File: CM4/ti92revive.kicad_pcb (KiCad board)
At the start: 2 copper layers, 205 x 116.7 mm, 200 parts, among them J1 USB_B, J2 Conn_01x02, J3 Conn_01x02, U1 Compute_Module_4_Connectors, U2 Compute_Module_4_Connectors, U3 BQ25887RGET

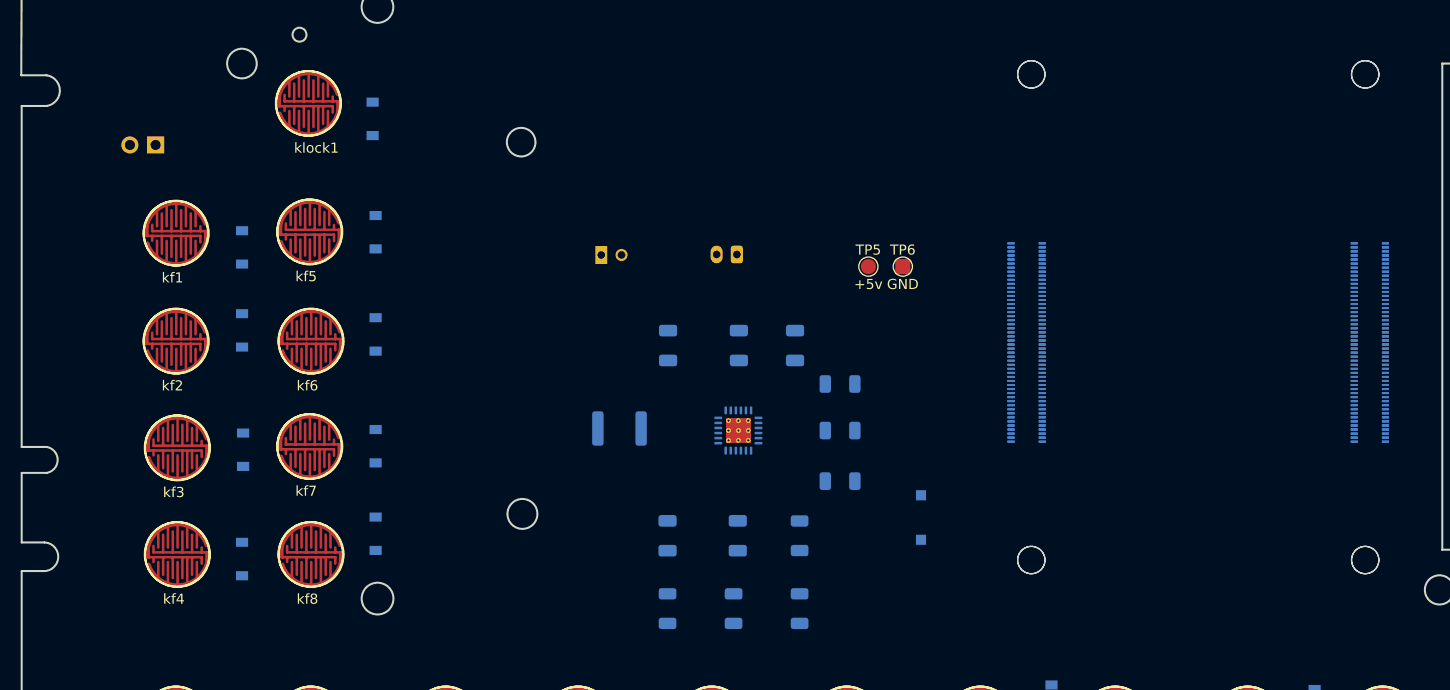
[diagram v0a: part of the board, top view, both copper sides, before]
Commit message: Laid out 5v ic and battery charger
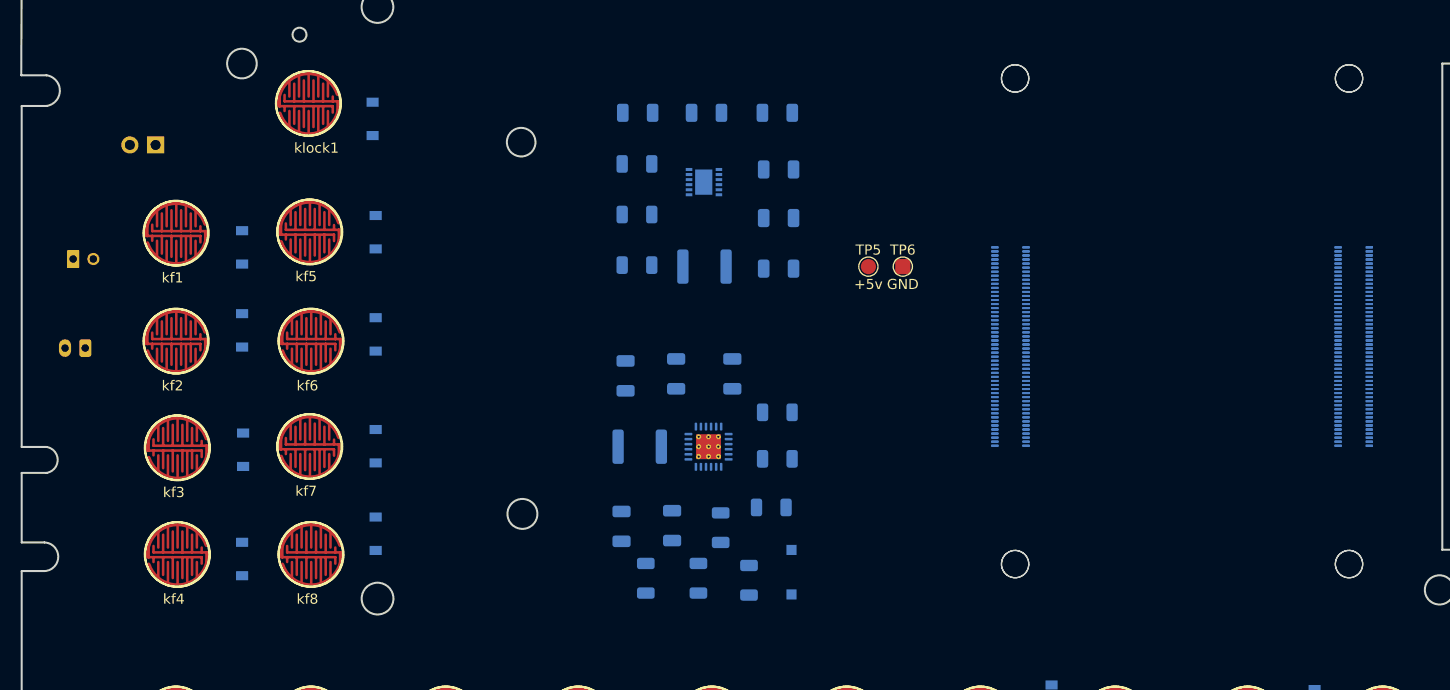
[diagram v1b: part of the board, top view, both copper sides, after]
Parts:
- added C10: .1uF, Capacitor_SMD:C_1206_3216Metric, B.Cu at (120.4, 50.8)
- added C11: 22uF, Capacitor_SMD:C_1206_3216Metric, B.Cu at (113.6, 50.8)
- added C6: 5.6nF, Capacitor_SMD:C_1206_3216Metric, B.Cu at (127.5, 61.2)
- added C7: 2.2uF, Capacitor_SMD:C_1206_3216Metric, B.Cu at (127.5, 56.4)
- added C8: 2.2uF, Capacitor_SMD:C_1206_3216Metric, B.Cu at (127.5, 66.2)
- added C9: .1uF, Capacitor_SMD:C_1206_3216Metric, B.Cu at (127.4, 50.8)
- added L2: 10uH, Inductor_SMD:L_1812_4532Metric, B.Cu at (120.2, 66.0)
- added R10: 105K, Resistor_SMD:R_1206_3216Metric, B.Cu at (113.5, 65.8)
- added R11: 23.2K, Resistor_SMD:R_1206_3216Metric, B.Cu at (113.5, 60.9)
- added R9: 4.7, Resistor_SMD:R_1206_3216Metric, B.Cu at (113.5, 55.9)
- added U4: MAX17643, trinamic-footprints:TDFN-12_3x3mm_P0.5mm, B.Cu at (120.1, 57.6)
- moved J3 65.1 mm to (59.0, 74.0)
- moved J2 52.2 mm to (59.8, 65.2)
- moved TP11 16.1 mm to (128.8, 98.4)
- moved TP10 12.8 mm to (128.8, 94.0)
- moved R8 10.4 mm to (119.6, 96.8)
- moved R4 9.18 mm to (114.4, 96.8)
- moved R1 8.52 mm to (124.6, 97.0)
- moved R2 7.84 mm to (121.8, 91.8)
- moved R3 7.28 mm to (126.8, 89.8)
- moved C4 6.80 mm to (123.0, 76.6)
- moved R6 6.80 mm to (127.4, 80.4)
- moved C2 6.80 mm to (117.4, 76.6)
- moved R5 6.80 mm to (127.4, 85.0)
- moved C1 6.57 mm to (117.0, 91.6)
- moved C5 5.16 mm to (112.4, 76.8)
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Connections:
- J1 pad 5: unconnected-(J1-Pad5) -> GND

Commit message: Added Power Button Control Circuit
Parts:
- added D82: PWR IND, LED_SMD:LED_2010_5025Metric, F.Cu at (243.0, 38.8)
- added JP1: Oopes just use a switch, Jumper:SolderJumper-2_P1.3mm_Open_RoundedPad1.0x1.5mm, B.Cu at (105.8, 67.0)
- added Q1: Q_NPN_BCE, Package_TO_SOT_SMD:SOT-23, B.Cu at (100.2, 66.8)
- added R12: 330, Resistor_SMD:R_1206_3216Metric, B.Cu at (99.2, 72.4)
- added R13: 330, Resistor_SMD:R_1206_3216Metric, B.Cu at (99.2, 77.6)
- added U5: ATTINY85-20PU, digikey-footprints:DIP-8_W7.62mm, B.Cu at (111.6, 71.2)
- D81: footprint LED_SMD:LED_1206_3216Metric -> LED_SMD:LED_2010_5025Metric
- moved C11 14.3 mm to (125.8, 43.4)
- moved L2 14.3 mm to (132.4, 58.6)
- moved C6 14.3 mm to (139.7, 53.8)
- moved C8 14.3 mm to (139.7, 58.8)
- moved C10 14.3 mm to (132.6, 43.4)
- moved C7 14.3 mm to (139.7, 49.0)
- moved C9 14.3 mm to (139.6, 43.4)
- moved R11 14.3 mm to (125.7, 53.5)
- moved R9 14.3 mm to (125.7, 48.5)
- moved U4 14.3 mm to (132.3, 50.2)
- moved R10 14.3 mm to (125.7, 58.5)
- moved R2 13.4 mm to (134.8, 95.2)
- moved R3 13.4 mm to (139.8, 93.2)
- moved C1 13.4 mm to (130.0, 95.0)
- moved C2 13.4 mm to (130.4, 80.0)
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- renumbered kbCTRL1 to kbPowerButton1
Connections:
- net Net-(C5-Pad2) renamed BAT+
- net Net-(J2-Pad1) renamed batCell+
- net Net-(U4-Pad1) renamed 5vRegulator
- D13 pad 2: Net-(D13-Pad2) -> unconnected-(D13-Pad2)
- kbPowerButton1 pad 1: col0 -> Net-(U5-Pad5)
- kbPowerButton1 pad 2: Net-(D13-Pad2) -> GND
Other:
- board text added: "Power Control"

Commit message: Added Power Control Relay
also cleaned up some junk and jank
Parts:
- removed U2: Compute_Module_4_Connectors, CM4:Raspberry-Pi-4-Compute-Module
- added D83: 1N4148W, Diode_SMD:D_SOD-123, B.Cu at (100.9, 95.8)
- added D84: 1N4148W, Diode_SMD:D_SOD-123, B.Cu at (100.9, 101.5)
- added U6: TQ2SA-L2-3V-Z-Remake, teensy:TQ2SA-L2-3V-Z, B.Cu at (111.2, 98.8)
- JP1: value Oopes just use a switch -> SolderJumper_2_Open
- Q1: value Q_NPN_BCE -> EMH3; footprint Package_TO_SOT_SMD:SOT-23 -> Package_TO_SOT_SMD:SOT-563
- moved Q1 2.51 mm to (97.9, 65.8), turned to 180 degrees
- moved R12 1.98 mm to (97.8, 71.0)
- moved U5 1.98 mm to (110.2, 69.8)
- moved JP1 1.98 mm to (104.4, 65.6)
- moved R13 1.98 mm to (97.8, 76.2)
- moved U1 1.80 mm to (167.3, 72.1)
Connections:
- Q1 pad 1: Net-(Q1-Pad1) -> GND
- Q1 pad 2: BAT+ -> SetPowerOFF
- Q1 pad 3: 5vRegulator -> Net-(U6-Pad5)
- R12 pad 1: Net-(Q1-Pad1) -> unconnected-(R12-Pad1)
- R12 pad 2: Net-(U5-Pad7) -> Net-(R12-Pad2)
- U1 pad 101: (no net) -> unconnected-(U1-Pad101)
- U1 pad 102: (no net) -> unconnected-(U1-Pad102)
- U1 pad 103: (no net) -> unconnected-(U1-Pad103)
- U1 pad 104: (no net) -> unconnected-(U1-Pad104)
- U1 pad 105: (no net) -> unconnected-(U1-Pad105)
- U1 pad 106: (no net) -> unconnected-(U1-Pad106)
- U1 pad 107: (no net) -> GND
- U1 pad 108: (no net) -> GND
- U1 pad 109: (no net) -> unconnected-(U1-Pad109)
- U1 pad 110: (no net) -> unconnected-(U1-Pad110)
- U1 pad 111: (no net) -> unconnected-(U1-Pad111)
- U1 pad 112: (no net) -> unconnected-(U1-Pad112)
- U1 pad 113: (no net) -> GND
- U1 pad 114: (no net) -> GND
- U1 pad 115: (no net) -> unconnected-(U1-Pad115)
- U1 pad 116: (no net) -> unconnected-(U1-Pad116)
- U1 pad 117: (no net) -> unconnected-(U1-Pad117)
- U1 pad 118: (no net) -> unconnected-(U1-Pad118)
- U1 pad 119: (no net) -> GND
- U1 pad 120: (no net) -> GND
- U1 pad 121: (no net) -> unconnected-(U1-Pad121)
- U1 pad 122: (no net) -> unconnected-(U1-Pad122)
- U1 pad 123: (no net) -> unconnected-(U1-Pad123)
- U1 pad 124: (no net) -> unconnected-(U1-Pad124)
- U1 pad 125: (no net) -> GND
- U1 pad 126: (no net) -> GND
- U1 pad 127: (no net) -> unconnected-(U1-Pad127)
- U1 pad 128: (no net) -> unconnected-(U1-Pad128)
- U1 pad 129: (no net) -> unconnected-(U1-Pad129)
- U1 pad 130: (no net) -> unconnected-(U1-Pad130)
- U1 pad 131: (no net) -> GND
- U1 pad 132: (no net) -> GND
- U1 pad 133: (no net) -> unconnected-(U1-Pad133)
- U1 pad 134: (no net) -> unconnected-(U1-Pad134)
- U1 pad 135: (no net) -> unconnected-(U1-Pad135)
- U1 pad 136: (no net) -> unconnected-(U1-Pad136)
- U1 pad 137: (no net) -> GND
- U1 pad 138: (no net) -> GND
- U1 pad 139: (no net) -> unconnected-(U1-Pad139)
- U1 pad 140: (no net) -> unconnected-(U1-Pad140)
- U1 pad 141: (no net) -> unconnected-(U1-Pad141)
- U1 pad 142: (no net) -> unconnected-(U1-Pad142)
- U1 pad 143: (no net) -> unconnected-(U1-Pad143)
- U1 pad 144: (no net) -> GND
- U1 pad 145: (no net) -> unconnected-(U1-Pad145)
- U1 pad 146: (no net) -> unconnected-(U1-Pad146)
- U1 pad 147: (no net) -> unconnected-(U1-Pad147)
- U1 pad 148: (no net) -> unconnected-(U1-Pad148)
- U1 pad 149: (no net) -> unconnected-(U1-Pad149)
- U1 pad 150: (no net) -> GND
- U1 pad 151: (no net) -> unconnected-(U1-Pad151)
- U1 pad 152: (no net) -> unconnected-(U1-Pad152)
- U1 pad 153: (no net) -> unconnected-(U1-Pad153)
- U1 pad 154: (no net) -> unconnected-(U1-Pad154)
- U1 pad 155: (no net) -> GND
- U1 pad 156: (no net) -> GND
- U1 pad 157: (no net) -> unconnected-(U1-Pad157)
- U1 pad 158: (no net) -> unconnected-(U1-Pad158)
- U1 pad 159: (no net) -> unconnected-(U1-Pad159)
- U1 pad 160: (no net) -> unconnected-(U1-Pad160)
- U1 pad 161: (no net) -> GND
- U1 pad 162: (no net) -> GND
- U1 pad 163: (no net) -> unconnected-(U1-Pad163)
- U1 pad 164: (no net) -> unconnected-(U1-Pad164)
- U1 pad 165: (no net) -> unconnected-(U1-Pad165)
- U1 pad 166: (no net) -> unconnected-(U1-Pad166)
- U1 pad 167: (no net) -> GND
- U1 pad 168: (no net) -> GND
- U1 pad 169: (no net) -> unconnected-(U1-Pad169)
- U1 pad 170: (no net) -> unconnected-(U1-Pad170)
- U1 pad 171: (no net) -> unconnected-(U1-Pad171)
- U1 pad 172: (no net) -> unconnected-(U1-Pad172)
- U1 pad 173: (no net) -> GND
- U1 pad 174: (no net) -> GND
- U1 pad 175: (no net) -> unconnected-(U1-Pad175)
- U1 pad 176: (no net) -> unconnected-(U1-Pad176)
- U1 pad 177: (no net) -> unconnected-(U1-Pad177)
- U1 pad 178: (no net) -> unconnected-(U1-Pad178)
- U1 pad 179: (no net) -> GND
- U1 pad 180: (no net) -> GND
- U1 pad 181: (no net) -> unconnected-(U1-Pad181)
- U1 pad 182: (no net) -> unconnected-(U1-Pad182)
- U1 pad 183: (no net) -> unconnected-(U1-Pad183)
- U1 pad 184: (no net) -> unconnected-(U1-Pad184)
- U1 pad 185: (no net) -> GND
- U1 pad 186: (no net) -> GND
- U1 pad 187: (no net) -> unconnected-(U1-Pad187)
- U1 pad 188: (no net) -> unconnected-(U1-Pad188)
- U1 pad 189: (no net) -> unconnected-(U1-Pad189)
- U1 pad 190: (no net) -> unconnected-(U1-Pad190)
- U1 pad 191: (no net) -> GND
- U1 pad 192: (no net) -> GND
- U1 pad 193: (no net) -> unconnected-(U1-Pad193)
- U1 pad 194: (no net) -> unconnected-(U1-Pad194)
- U1 pad 195: (no net) -> unconnected-(U1-Pad195)
- U1 pad 196: (no net) -> unconnected-(U1-Pad196)
- U1 pad 197: (no net) -> GND
- U1 pad 198: (no net) -> GND
- U1 pad 199: (no net) -> unconnected-(U1-Pad199)
- U1 pad 200: (no net) -> unconnected-(U1-Pad200)
- U1 pad 77: Net-(U1-Pad77) -> +5
- U1 pad 79: Net-(U1-Pad77) -> +5
- U1 pad 81: Net-(U1-Pad77) -> +5
- U1 pad 83: Net-(U1-Pad77) -> +5
- U1 pad 85: Net-(U1-Pad77) -> +5
- U1 pad 87: Net-(U1-Pad77) -> +5
- U5 pad 2: unconnected-(U5-Pad2) -> SetPowerOFF
- U5 pad 7: Net-(U5-Pad7) -> SetPowerON

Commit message: Wrote program discription
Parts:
- R7: moved to B.Cu
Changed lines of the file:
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@@
       (net 90 "Net-(D34-Pad2)") (pinfunction "2") (pintype "passive") (zone_connect 2))
   )
-  (footprint "Resistor_SMD:R_1206_3216Metric" (layer "F.Cu")
-    (at 226.8 52.4 -90)
-    (descr "Resistor SMD 1206 (3216 Metric), square (rectangular) end terminal, IPC_7351 nominal, (Body size source: IPC-SM-782 page 72, https://www.pcb-3d.com/wordpress/wp-content/uploads/ipc-sm-782a_amendment_1_and_2.pdf), generated with kicad-footprint-generator")
-    (tags "resistor")
-    (property "Sheetfile" "ps.kicad_sch")
-    (property "Sheetname" "PowerSupply")
-    (attr smd)
-    (fp_text reference "R7" (at 0 -1.82 90) (layer "F.SilkS")
-      (effects (font (size 1 1) (thickness 0.15)))
-    )
-    (fp_text value "10K" (at 0 1.82 90) (layer "F.Fab")
-      (effects (font (size 1 1) (thickness 0.15)))
-    )
-    (fp_text user "${REFERENCE}" (at 0 0 90) (layer "F.Fab")
-      (effects (font (size 0.8 0.8) (thickness 0.12)))
-    )
-    (fp_line (start -0.727064 -0.91) (end 0.727064 -0.91) (layer "F.SilkS") (width 0.12))
-    (fp_line (start -0.727064 0.91) (end 0.727064 0.91) (layer "F.SilkS") (width 0.12))
-    (fp_line (start 2.28 1.12) (end -2.28 1.12) (layer "F.CrtYd") (width 0.05))
-    (fp_line (start -2.28 1.12) (end -2.28 -1.12) (layer "F.CrtYd") (width 0.05))
-    (fp_line (start -2.28 -1.12) (end 2.28 -1.12) (layer "F.CrtYd") (width 0.05))
-    (fp_line (start 2.28 -1.12) (end 2.28 1.12) (layer "F.CrtYd") (width 0.05))
-    (fp_line (start 1.6 -0.8) (end 1.6 0.8) (layer "F.Fab") (width 0.1))
-    (fp_line (start -1.6 0.8) (end -1.6 -0.8) (layer "F.Fab") (width 0.1))
-    (fp_line (start 1.6 0.8) (end -1.6 0.8) (layer "F.Fab") (width 0.1))
-    (fp_line (start -1.6 -0.8) (end 1.6 -0.8) (layer "F.Fab") (width 0.1))
-    (pad "1" smd roundrect (at -1.4625 0 270) (locked) (size 1.125 1.75) (layers "F.Cu" "F.Paste" "F.Mask") (roundrect_rratio 0.222222)
-      (net 182 "Net-(D81-Pad2)") (pintype "passive"))
-    (pad "2" smd roundrect (at 1.4625 0 270) (locked) (size 1.125 1.75) (layers "F.Cu" "F.Paste" "F.Mask") (roundrect_rratio 0.222222)
-      (net 187 "CCVref") (pintype "passive"))
-    (model "${KISYS3DMOD}/Resistor_SMD.3dshapes/R_1206_3216Metric.wrl"
-      (offset (xyz 0 0 0))
-      (scale (xyz 1 1 1))
-      (rotate (xyz 0 0 0))
-    )
-  )
   (footprint "18650:Kbpad" (layer "F.Cu")
     (at 147.32 110.617)
@@
       (offset (xyz 0 0 0))
       (scale (xyz 1 1 1))
+      (rotate (xyz 0 0 0))
+    )
+  )
+  (footprint "Resistor_SMD:R_1206_3216Metric" (layer "B.Cu")
+    (at 226.8 52.4 -90)
+    (descr "Resistor SMD 1206 (3216 Metric), square (rectangular) end terminal, IPC_7351 nominal, (Body size source: IPC-SM-782 page 72, https://www.pcb-3d.com/wordpress/wp-content/uploads/ipc-sm-782a_amendment_1_and_2.pdf), generated with kicad-footprint-generator")
+    (tags "resistor")
+    (property "Sheetfile" "ps.kicad_sch")
+    (property "Sheetname" "PowerSupply")
+    (attr smd)
+    (fp_text reference "R7" (at 0 1.82 -90) (layer "B.SilkS")
+      (effects (font (size 1 1) (thickness 0.15)) (justify mirror))
+    )
+    (fp_text value "10K" (at 0 -1.82 -90) (layer "B.Fab")
+      (effects (font (size 1 1) (thickness 0.15)) (justify mirror))
+    )
+    (fp_text user "${REFERENCE}" (at 0 0 -90) (layer "B.Fab")
+      (effects (font (size 0.8 0.8) (thickness 0.12)) (justify mirror))
+    )
+    (fp_line (start -0.727064 0.91) (end 0.727064 0.91) (layer "B.SilkS") (width 0.12))
+    (fp_line (start -0.727064 -0.91) (end 0.727064 -0.91) (layer "B.SilkS") (width 0.12))
+    (fp_line (start 2.28 -1.12) (end -2.28 -1.12) (layer "B.CrtYd") (width 0.05))
+    (fp_line (start -2.28 -1.12) (end -2.28 1.12) (layer "B.CrtYd") (width 0.05))
+    (fp_line (start -2.28 1.12) (end 2.28 1.12) (layer "B.CrtYd") (width 0.05))
+    (fp_line (start 2.28 1.12) (end 2.28 -1.12) (layer "B.CrtYd") (width 0.05))
+    (fp_line (start 1.6 0.8) (end 1.6 -0.8) (layer "B.Fab") (width 0.1))
+    (fp_line (start -1.6 -0.8) (end -1.6 0.8) (layer "B.Fab") (width 0.1))
+    (fp_line (start 1.6 -0.8) (end -1.6 -0.8) (layer "B.Fab") (width 0.1))
+    (fp_line (start -1.6 0.8) (end 1.6 0.8) (layer "B.Fab") (width 0.1))
+    (pad "1" smd roundrect (at -1.4625 0 270) (locked) (size 1.125 1.75) (layers "B.Cu" "B.Paste" "B.Mask") (roundrect_rratio 0.222222)
+      (net 182 "Net-(D81-Pad2)") (pintype "passive"))
+    (pad "2" smd roundrect (at 1.4625 0 270) (locked) (size 1.125 1.75) (layers "B.Cu" "B.Paste" "B.Mask") (roundrect_rratio 0.222222)
+      (net 187 "CCVref") (pintype "passive"))
+    (model "${KISYS3DMOD}/Resistor_SMD.3dshapes/R_1206_3216Metric.wrl"
+      (offset (xyz 0 0 0))
+      (scale (xyz 1 1 1))
